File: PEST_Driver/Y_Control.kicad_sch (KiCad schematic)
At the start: 68 parts, among them J1 Conn_01x02, J2 Conn_01x02, J3 Conn_01x02, J4 Conn_01x02, J5 Conn_01x02, J6 Conn_01x02, J7 Conn_01x02, J8 Conn_01x02, U19 74HC4051, U2 74HC4051, U20 74HC4051, U21 74HC595, U22 74HC4051, U3 74HC4051

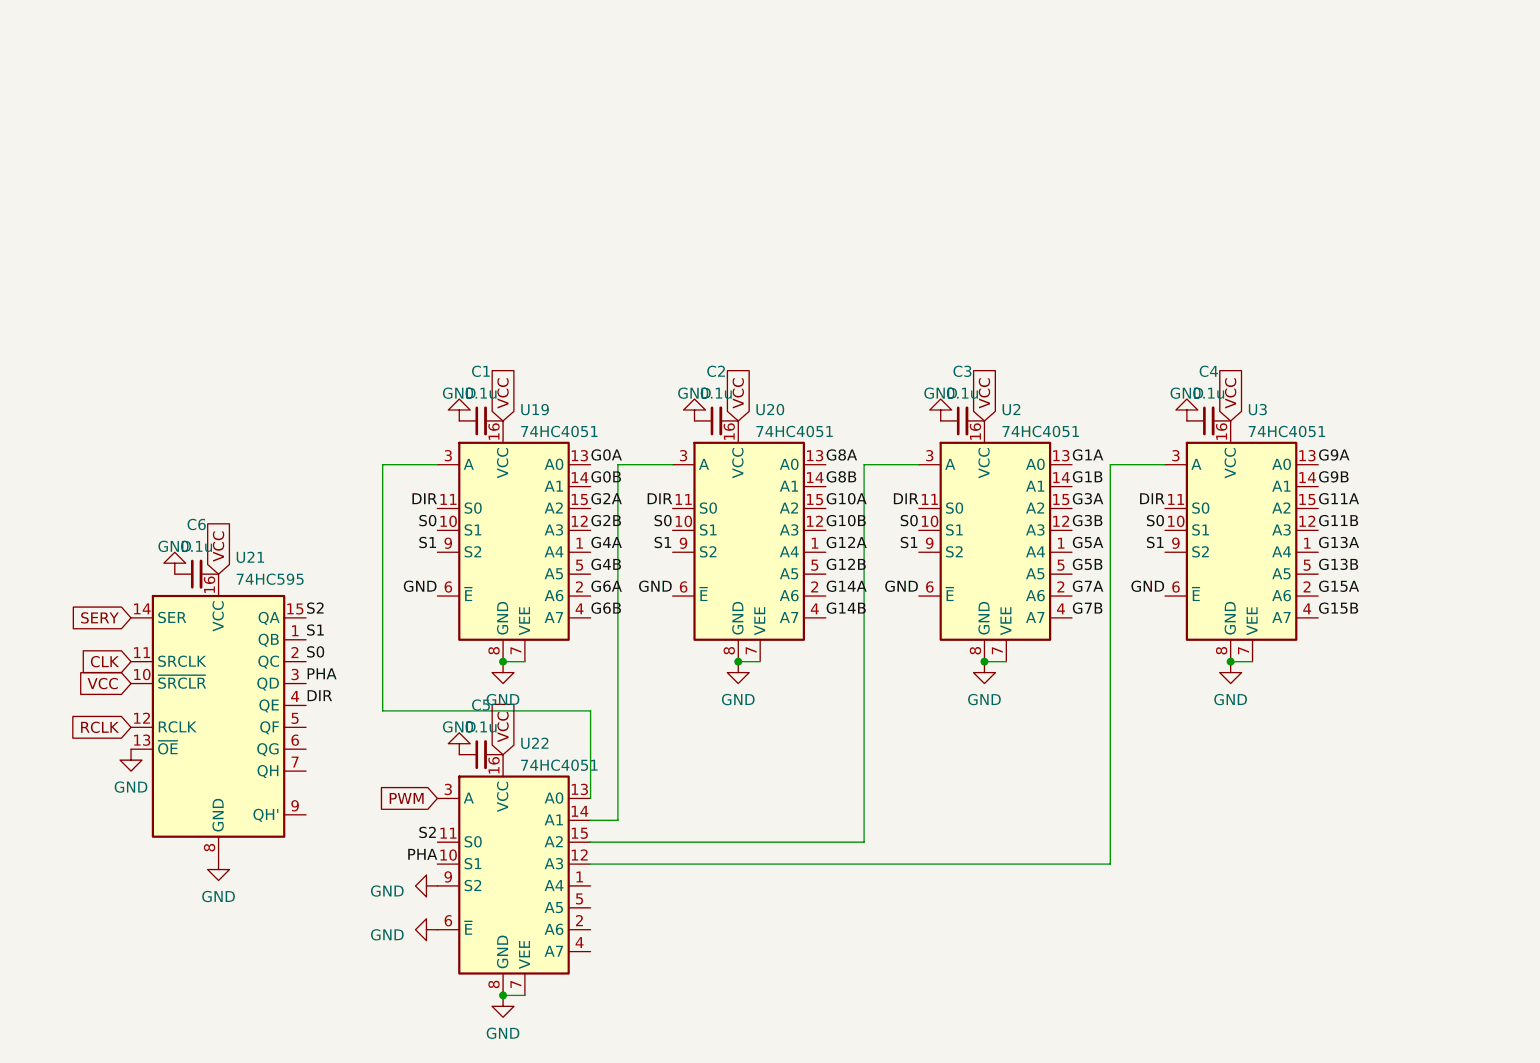
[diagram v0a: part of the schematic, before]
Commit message: Added independent signal ground to schematic
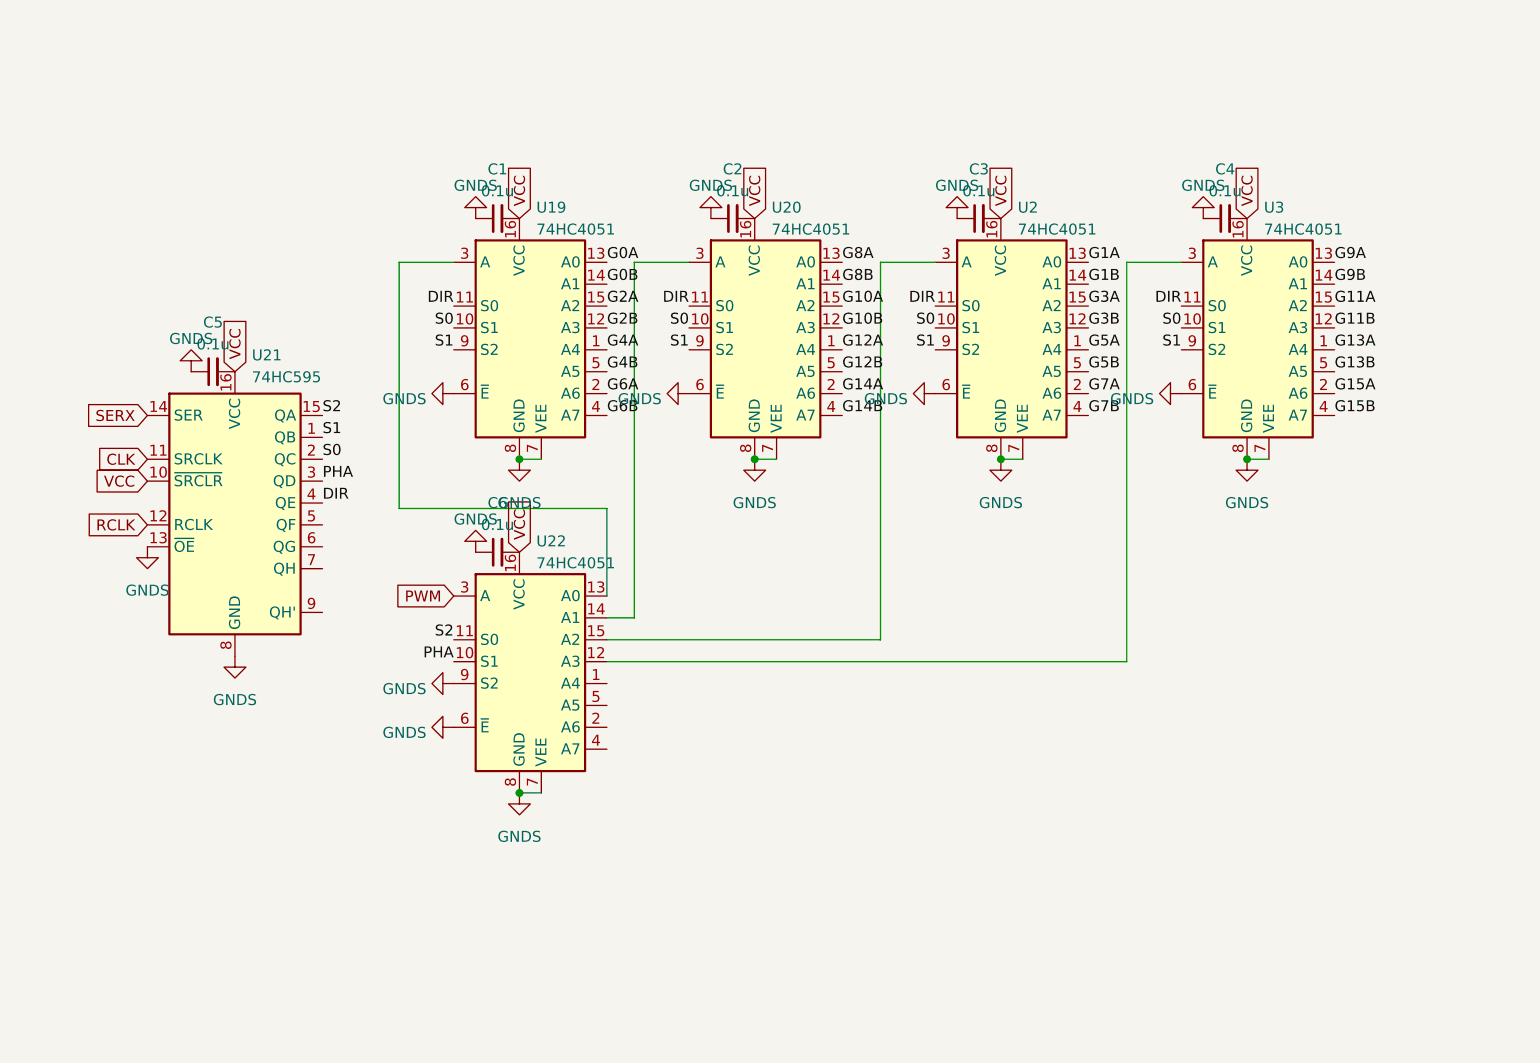
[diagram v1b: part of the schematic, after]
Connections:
- net GND: no longer C1.1, C2.1, C3.1, C4.1, C5.1, C6.1, U19.6 (~{E}), U19.7 (VEE), U19.8 (GND), U2.6 (~{E}), U2.7 (VEE), U2.8 (GND), U20.6 (~{E}), U20.7 (VEE), U20.8 (GND), U21.13 (~{OE}), U21.8 (GND), U22.6 (~{E}), U22.7 (VEE), U22.8 (GND), U22.9 (S2), U3.6 (~{E}), U3.7 (VEE), U3.8 (GND)
- net SERY renamed SERX
- new net GNDS: C1.1, C2.1, C3.1, C4.1, C5.1, C6.1, U19.6 (~{E}), U19.7 (VEE), U19.8 (GND), U2.6 (~{E}), U2.7 (VEE), U2.8 (GND), U20.6 (~{E}), U20.7 (VEE), U20.8 (GND), U21.13 (~{OE}), U21.8 (GND), U22.6 (~{E}), U22.7 (VEE), U22.8 (GND), U22.9 (S2), U3.6 (~{E}), U3.7 (VEE), U3.8 (GND)

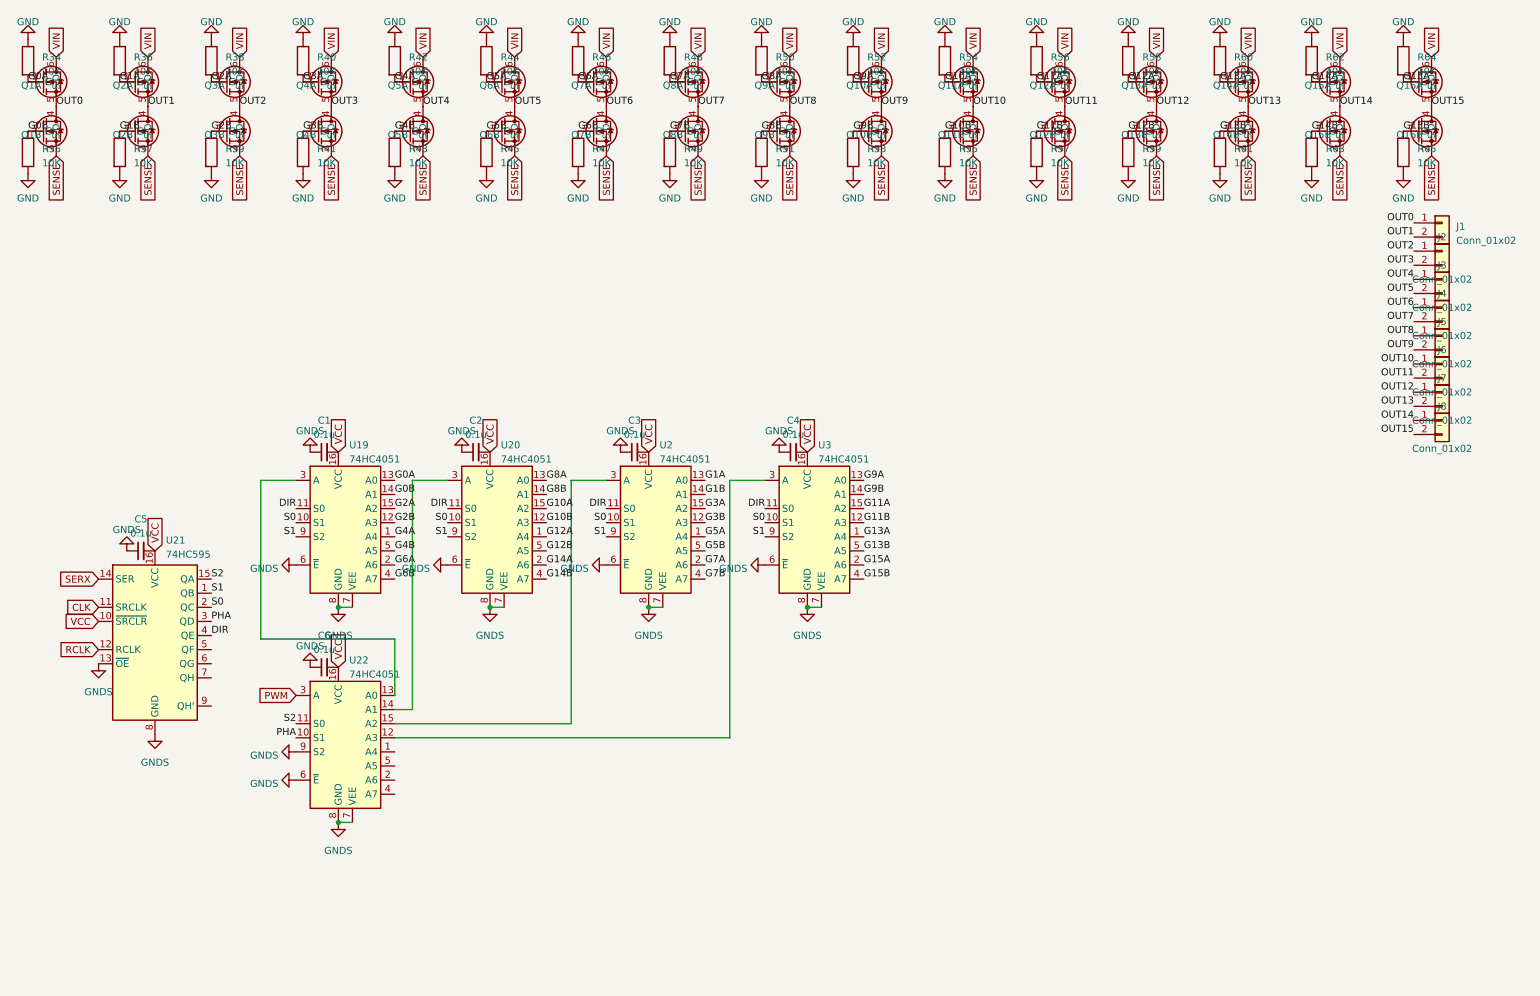
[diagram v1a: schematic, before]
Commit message: Finished wiring independent MOSFET and logic grounds
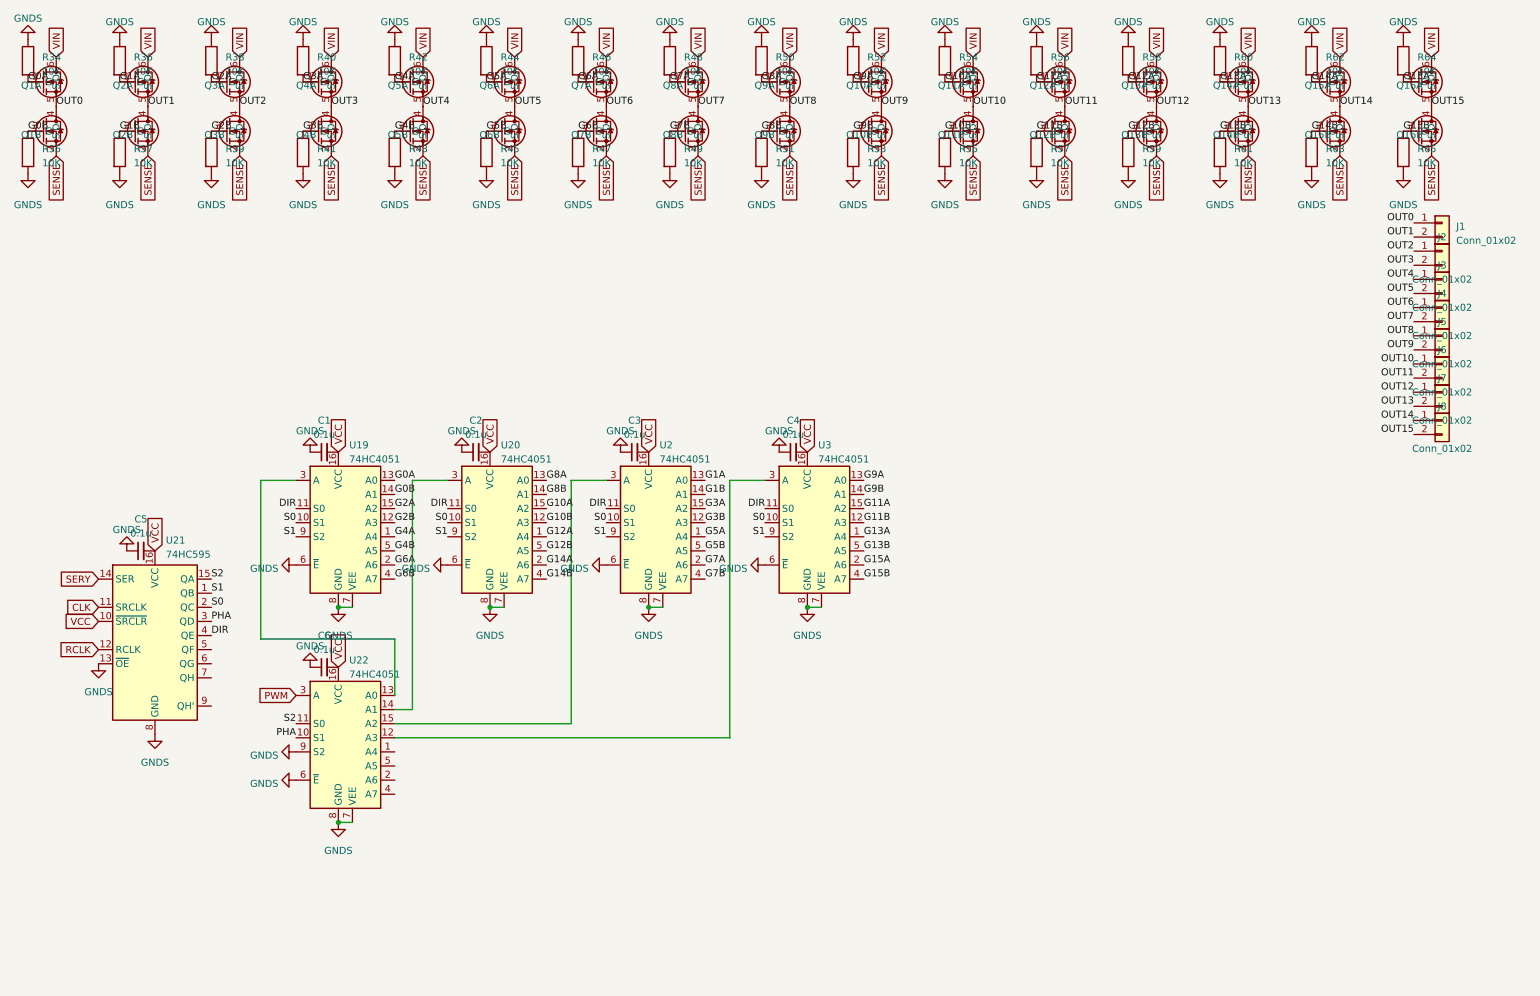
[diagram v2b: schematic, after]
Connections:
- net GND is gone; now on net GNDS: R34.1, R35.2, R36.1, R37.2, R38.1, R39.2, R40.1, R41.2, R42.1, R43.2, R44.1, R45.2, R46.1, R47.2, R48.1, R49.2, R50.1, R51.2, R52.1, R53.2, R54.1, R55.2, R56.1, R57.2, R58.1, R59.2, R60.1, R61.2, R62.1, R63.2, R64.1, R65.2
- net SERX renamed SERY

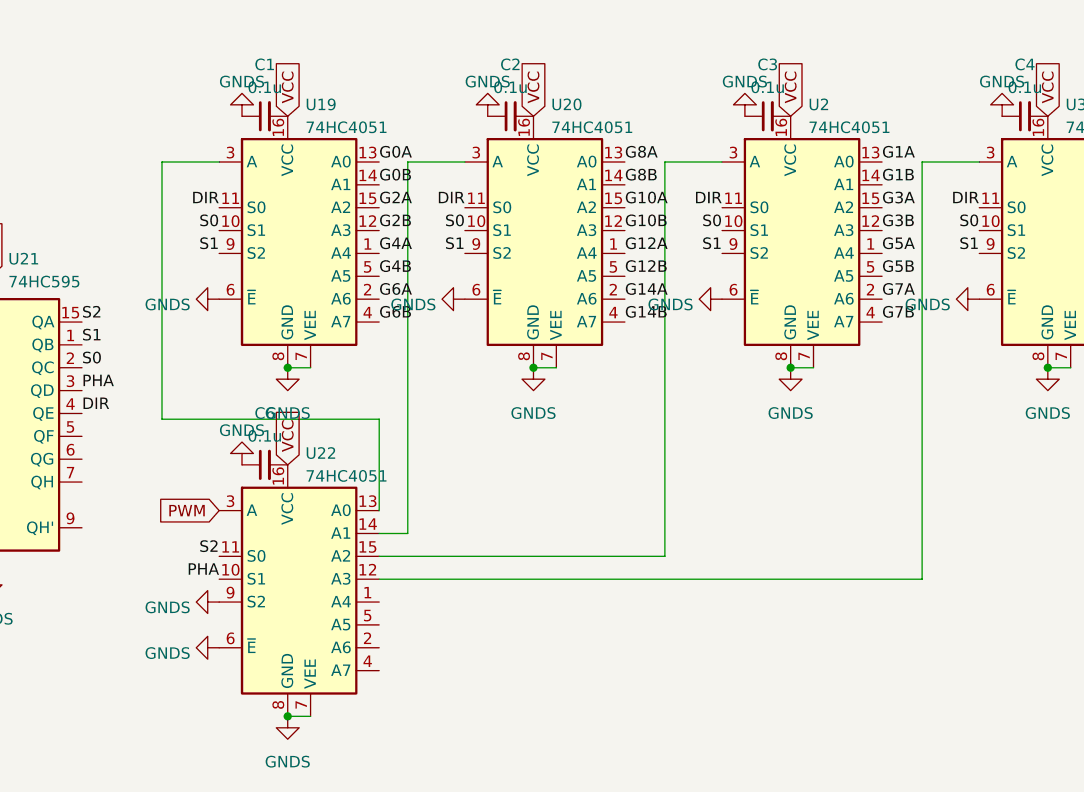
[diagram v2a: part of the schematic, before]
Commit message: Added more pulldown resistors to PEST Driver
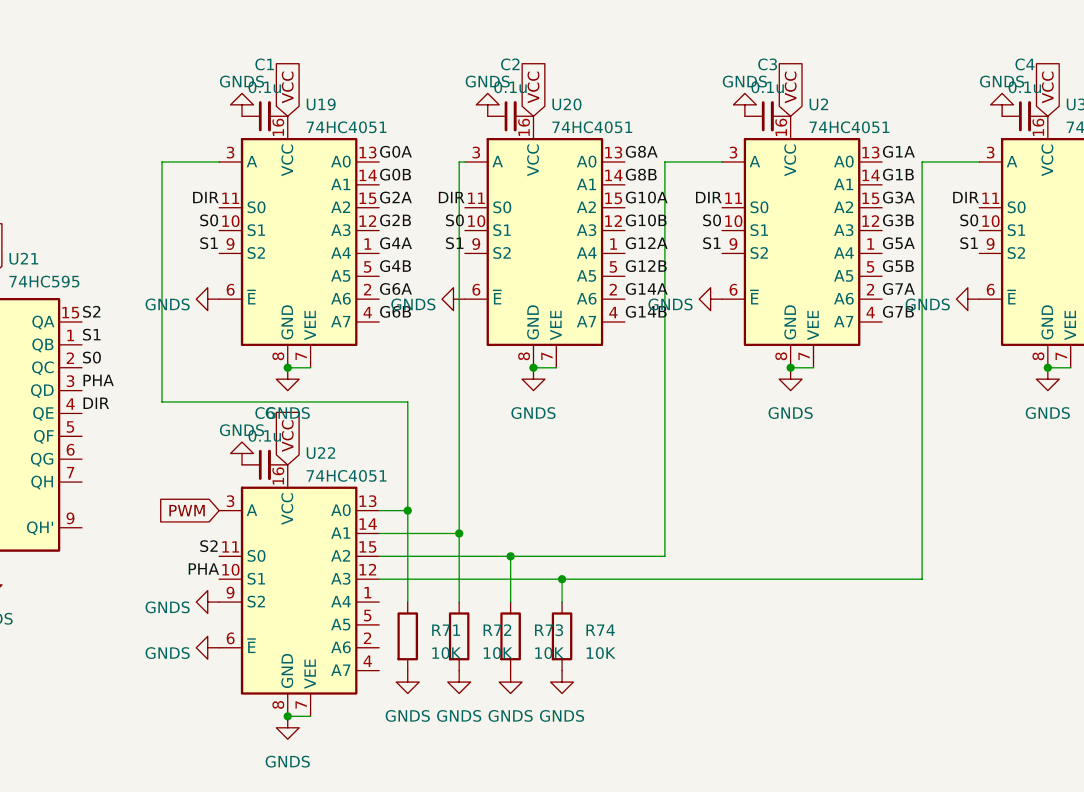
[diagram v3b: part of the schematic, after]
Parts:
- added R71, R72, R73, R74: 10K, Resistor_SMD:R_0402_1005Metric, symbol Device:R
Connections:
- net GNDS: now also R71.2, R72.2, R73.2, R74.2
- net at U22.12 (A3), U3.3 (A): now also R74.1
- net at U19.3 (A), U22.13 (A0): now also R71.1
- net at U20.3 (A), U22.14 (A1): now also R72.1
- net at U2.3 (A), U22.15 (A2): now also R73.1
